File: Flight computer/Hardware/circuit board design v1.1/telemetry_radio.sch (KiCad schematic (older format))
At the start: 15 parts, among them J7 Conn_Coaxial, U2 0433BM41A0019E, U3 Si4463, X1 TM-32.000-AF3-33-S-Oscillator

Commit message: put in new acclerometers and 9dof sensor. Changed supplier from mouser to farnell and RS
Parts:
- J7: Cost 0.746 -> 0.617; Purchase link https://uk.farnell.com/hirose-hrs/u-fl-r-smt-1-10/rf-coaxia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 -> https://uk.rs-online.com/web/p/coaxial-plugs-sockets/702542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
- U2: symbol 0433BM41A0019E:0433BM41A0019E -> circuit-board-design-rescue:0433BM41A0019E-0433BM41A0019E; min_quantity (none) -> 1
- X1: min_quantity (none) -> 2
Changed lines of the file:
@@
 F 2 "Connector_Coaxial:U.FL_Hirose_U.FL-R-SMT-1_Vertical" H 8200 5300 50  0001 C CNN
 F 3 "https://www.mouser.co.uk/datasheet/2/185/U.FL_catalog-939761.pdf" H 8200 5300 50  0001 C CNN
-F 4 "0.746" H 8200 5300 50  0001 C CNN "Cost"
-F 5 "https://uk.farnell.com/hirose-hrs/u-fl-r-smt-1-10/rf-coaxial-u-fl-straight-jack/dp/1688077?st=ufl" H 8200 5300 50  0001 C CNN "Purchase link"
+F 4 "0.617" H 8200 5300 50  0001 C CNN "Cost"
+F 5 "https://uk.rs-online.com/web/p/coaxial-plugs-sockets/7025425/" H 8200 5300 50  0001 C CNN "Purchase link"
 F 6 "10" H 8200 5300 50  0001 C CNN "min_quantity"
 	1    8200 5300
@@
 $EndComp
 $Comp
-L 0433BM41A0019E:0433BM41A0019E U2
+L circuit-board-design-rescue:0433BM41A0019E-0433BM41A0019E U2
 U 1 1 5D767292
 P 6350 4450
+AR Path="/5D767292" Ref="U2"  Part="1"
+AR Path="/5D5B17D8/5D767292" Ref="U2"  Part="1"
 F 0 "U2" H 6350 4967 50  0000 C CNN
 F 1 "0433BM41A0019E" H 6350 4876 50  0000 C CNN
@@
 F 4 "0.745" H 6350 4450 50  0001 C CNN "Cost"
 F 5 "https://www.mouser.co.uk/ProductDetail/Johanson-Technology/0433BM41A0019E?qs=cgWa3jCOTNkHeQmiwnsqmQ==" H 6350 4450 50  0001 C CNN "Purchase link"
+F 6 "1" H 6350 4450 50  0001 C CNN "min_quantity"
 	1    6350 4450
 	1    0    0    -1
@@
 F 4 "3.43" H 1550 3600 50  0001 C CNN "Cost"
 F 5 "https://uk.rs-online.com/web/p/tcxo-oscillators/1442366/" H 1550 3600 50  0001 C CNN "Purchase link"
+F 6 "2" H 1550 3600 50  0001 C CNN "min_quantity"
 	1    1550 3600
 	1    0    0    -1

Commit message: Fully routed board v1.1 with the new high g accelerometer
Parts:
- C20, C21: footprint Capacitor_SMD:C_0402_1005Metric -> Capacitor_SMD:C_0603_1608Metric
- X1: footprint Crystal:Crystal_SMD_2520-4Pin_2.5x2.0mm -> flight-computer:Crystal_SMD_2520-4Pin_2.5x2.0mm
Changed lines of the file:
@@
 F 0 "X1" H 1500 4800 50  0000 L CNN
 F 1 "TM-32.000-AF3-33-S-Oscillator" H 1000 4700 50  0000 L CNN
-F 2 "Crystal:Crystal_SMD_2520-4Pin_2.5x2.0mm" H 2000 3250 50  0001 C CNN
+F 2 "flight-computer:Crystal_SMD_2520-4Pin_2.5x2.0mm" H 2000 3250 50  0001 C CNN
 F 3 "https://docs-emea.rs-online.com/webdocs/15dc/0900766b815dc7d9.pdf" H 1450 3600 50  0001 C CNN
 F 4 "3.43" H 1550 3600 50  0001 C CNN "Cost"
@@
 F 0 "C21" H 1050 3500 50  0000 C CNN
 F 1 "33nF" H 1050 3400 50  0000 C CNN
-F 2 "Capacitor_SMD:C_0402_1005Metric" H 800 3500 50  0001 C CNN
+F 2 "Capacitor_SMD:C_0603_1608Metric" H 800 3500 50  0001 C CNN
 F 3 "~" H 800 3500 50  0001 C CNN
 	1    800  3500
@@
 F 0 "C20" H 2550 3900 50  0000 C CNN
 F 1 "10nF" H 2550 3800 50  0000 C CNN
-F 2 "Capacitor_SMD:C_0402_1005Metric" H 2300 3900 50  0001 C CNN
+F 2 "Capacitor_SMD:C_0603_1608Metric" H 2300 3900 50  0001 C CNN
 F 3 "~" H 2300 3900 50  0001 C CNN
 	1    2300 3900

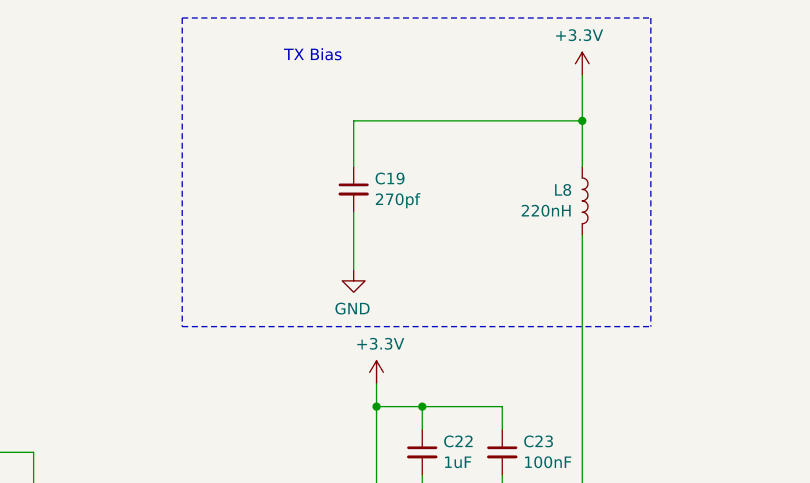
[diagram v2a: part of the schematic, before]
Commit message: put in logo for V1.1
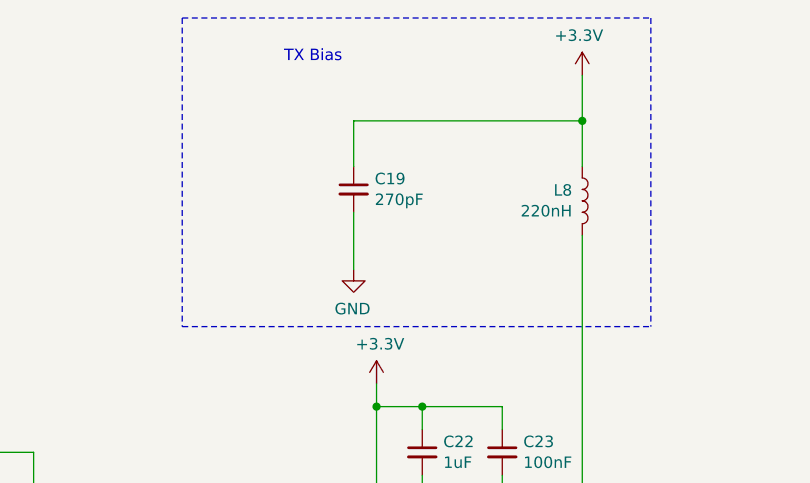
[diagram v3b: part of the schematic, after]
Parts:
- C19: value 270pf -> 270pF
- C20: Cost (none) -> 0.031; Purchase link (none) -> https://uk.rs-online.com/web/p/mlccs-multilayer-ceramic-cap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; min_quantity (none) -> 100
- C22: Cost (none) -> 0.01; Purchase link (none) -> https://uk.rs-online.com/web/p/mlccs-multilayer-ceramic-cap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; min_quantity (none) -> 250
- C23: Cost (none) -> 0.01; Purchase link (none) -> https://uk.rs-online.com/web/p/mlccs-multilayer-ceramic-cap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; min_quantity (none) -> 50
- L8: Cost (none) -> 0.126; Purchase link (none) -> https://uk.rs-online.com/web/p/multilayer-surface-mount-ind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; min_quantity (none) -> 10
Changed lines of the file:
@@
 P 3700 2450
 F 0 "C19" H 3608 2496 50  0000 R CNN
-F 1 "270pf" H 3608 2405 50  0000 R CNN
+F 1 "270pF" H 3608 2405 50  0000 R CNN
 F 2 "Capacitor_SMD:C_0402_1005Metric" H 3700 2450 50  0001 C CNN
 F 3 "~" H 3700 2450 50  0001 C CNN
@@
 F 2 "Inductor_SMD:L_0603_1608Metric" H 4700 2500 50  0001 C CNN
 F 3 "~" H 4700 2500 50  0001 C CNN
+F 4 "0.126" H 4700 2500 50  0001 C CNN "Cost"
+F 5 "https://uk.rs-online.com/web/p/multilayer-surface-mount-inductors/6041209/" H 4700 2500 50  0001 C CNN "Purchase link"
+F 6 "10" H 4700 2500 50  0001 C CNN "min_quantity"
 	1    4700 2500
 	1    0    0    1
@@
 F 1 "100nF" H 4258 3555 50  0000 R CNN
 F 2 "Capacitor_SMD:C_0603_1608Metric" H 4350 3600 50  0001 C CNN
-F 3 "~" H 4350 3600 50  0001 C CNN
+F 3 "https://docs-emea.rs-online.com/webdocs/0dc2/0900766b80dc2409.pdf" H 4350 3600 50  0001 C CNN
+F 4 "0.01" H 4350 3600 50  0001 C CNN "Cost"
+F 5 "https://uk.rs-online.com/web/p/mlccs-multilayer-ceramic-capacitors/6983251/" H 4350 3600 50  0001 C CNN "Purchase link"
+F 6 "50" H 4350 3600 50  0001 C CNN "min_quantity"
 	1    4350 3600
 	-1   0    0    -1
@@
 F 2 "Capacitor_SMD:C_0603_1608Metric" H 4000 3600 50  0001 C CNN
 F 3 "~" H 4000 3600 50  0001 C CNN
+F 4 "0.01" H 4000 3600 50  0001 C CNN "Cost"
+F 5 "https://uk.rs-online.com/web/p/mlccs-multilayer-ceramic-capacitors/1358359/" H 4000 3600 50  0001 C CNN "Purchase link"
+F 6 "250" H 4000 3600 50  0001 C CNN "min_quantity"
 	1    4000 3600
 	-1   0    0    -1
@@
 F 2 "Capacitor_SMD:C_0603_1608Metric" H 2300 3900 50  0001 C CNN
 F 3 "~" H 2300 3900 50  0001 C CNN
+F 4 "0.031" H 2300 3900 50  0001 C CNN "Cost"
+F 5 "https://uk.rs-online.com/web/p/mlccs-multilayer-ceramic-capacitors/8391727/" H 2300 3900 50  0001 C CNN "Purchase link"
+F 6 "100" H 2300 3900 50  0001 C CNN "min_quantity"
 	1    2300 3900
 	1    0    0    1

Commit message: updated links to purchase
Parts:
- C21: Cost (none) -> 0.008; Purchase link (none) -> https://uk.rs-online.com/web/p/mlccs-multilayer-ceramic-cap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; min_quantity (none) -> 100
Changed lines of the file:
@@
 F 2 "Capacitor_SMD:C_0603_1608Metric" H 800 3500 50  0001 C CNN
 F 3 "~" H 800 3500 50  0001 C CNN
+F 4 "0.008" H 800 3500 50  0001 C CNN "Cost"
+F 5 "https://uk.rs-online.com/web/p/mlccs-multilayer-ceramic-capacitors/8392805/" H 800 3500 50  0001 C CNN "Purchase link"
+F 6 "100" H 800 3500 50  0001 C CNN "min_quantity"
 	1    800  3500
 	1    0    0    1

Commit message: put in the last bom purchase links
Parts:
- C19, C9: Cost (none) -> 0.01; Purchase link (none) -> https://uk.rs-online.com/web/p/mlccs-multilayer-ceramic-cap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; min_quantity (none) -> 200
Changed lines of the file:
@@
 F 2 "Capacitor_SMD:C_0402_1005Metric" H 7800 4250 50  0001 C CNN
 F 3 "~" H 7800 4250 50  0001 C CNN
+F 4 "0.01" H 7800 4250 50  0001 C CNN "Cost"
+F 5 "https://uk.rs-online.com/web/p/mlccs-multilayer-ceramic-capacitors/9155553/" H 7800 4250 50  0001 C CNN "Purchase link"
+F 6 "200" H 7800 4250 50  0001 C CNN "min_quantity"
 	1    7800 4250
 	0    1    -1   0
@@
 F 2 "Capacitor_SMD:C_0402_1005Metric" H 3700 2450 50  0001 C CNN
 F 3 "~" H 3700 2450 50  0001 C CNN
+F 4 "0.01" H 3700 2450 50  0001 C CNN "Cost"
+F 5 "https://uk.rs-online.com/web/p/mlccs-multilayer-ceramic-capacitors/9155553/" H 3700 2450 50  0001 C CNN "Purchase link"
+F 6 "200" H 3700 2450 50  0001 C CNN "min_quantity"
 	1    3700 2450
 	-1   0    0    -1
